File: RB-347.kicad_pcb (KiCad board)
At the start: 2 copper layers, 30 x 55 mm, 34 parts, among them J1 Conn_USB_C_Socket, J2 PINHD_1x10_Male, J3 PINHD_1x10_Male, J4 PINHD_1x10_Male, SW1 I2C, SW2 SPDT_Slide_SMD_6.7x2.6mm, U1 USBLC6-2SC6, U2 CH347F, U3 TLV74333PDBVR, U4 TLV74318PDBVR, Y1 8Mhz

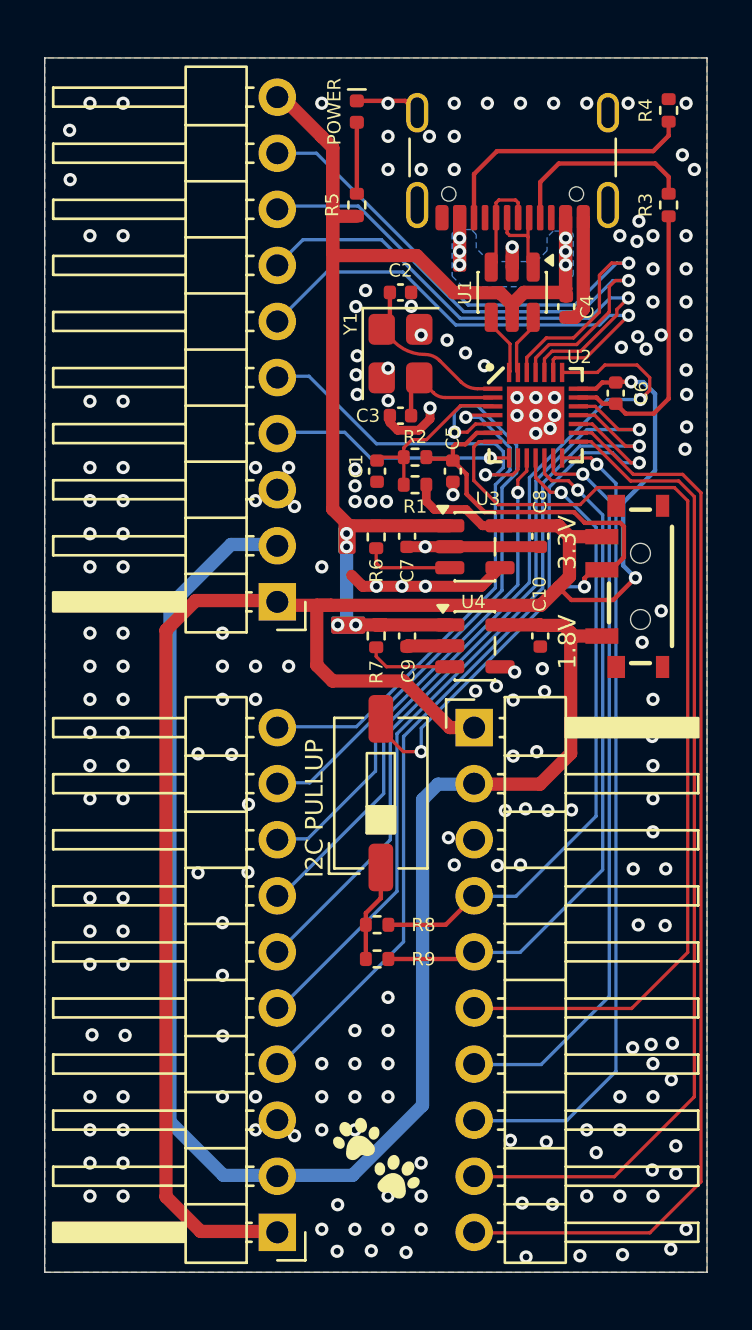
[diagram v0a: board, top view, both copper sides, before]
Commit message: add I²C indicator LED
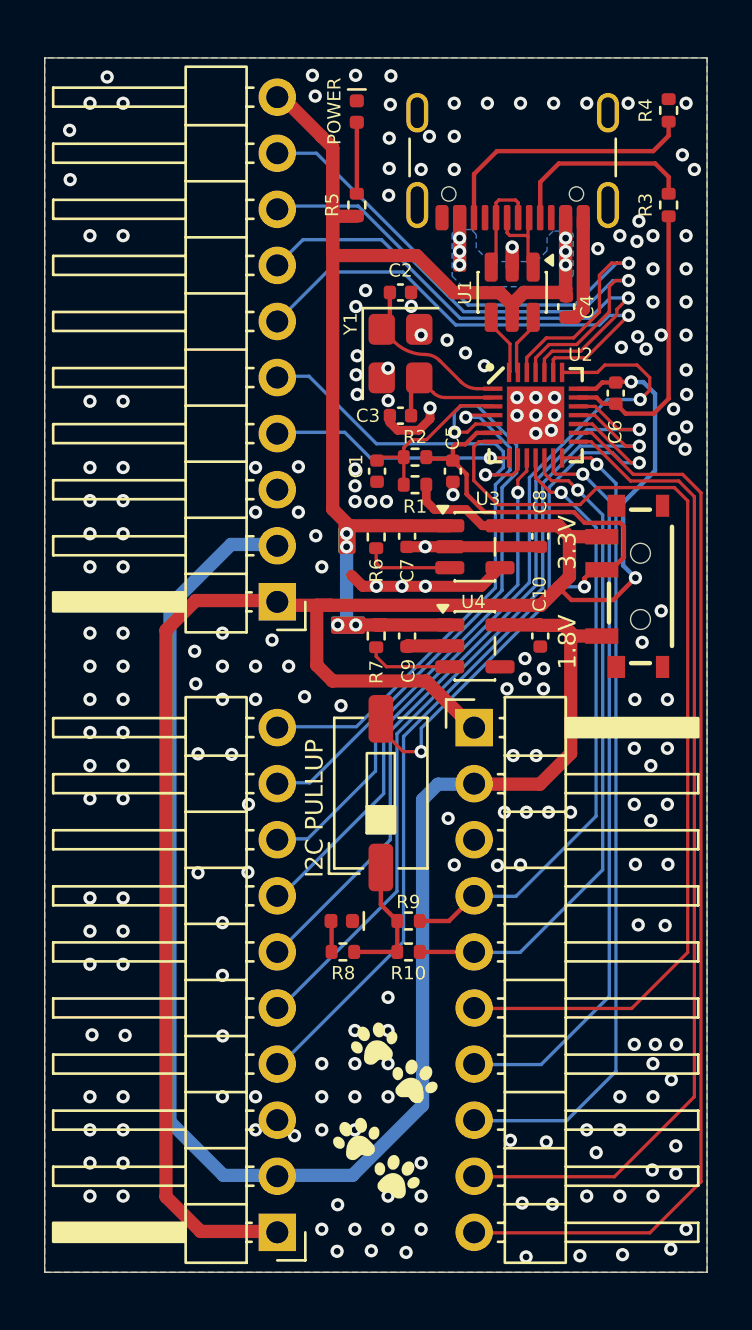
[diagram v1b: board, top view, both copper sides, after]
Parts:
- added G***: LOGO, LOGO, F.Cu at (122.9, 112.8)
- added LED2: POWER, PCM_SparkFun-LED:LED_0402_1005Metric_Red, F.Cu at (120.5, 106.3)
- added R8: 1k, Resistor_SMD:R_0402_1005Metric, F.Cu at (120.6, 107.8)
- moved R10 1.46 mm to (123.6, 107.8)
- moved R9 1.43 mm to (123.6, 106.3)
- renumbered R9 to R10, R8 to R9
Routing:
- net GND: track 41.8 -> 38.9 mm, vias 212 -> 228
- net Net-(R10-Pad1): track 4.47 -> 6.09 mm
- net CTS1/SCL: track 29.1 -> 27.6 mm
- net Net-(LED2-A): track 0.00 -> 1.41 mm
- net RTS1/SDA: track 31.6 -> 30.4 mm

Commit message: change connectors
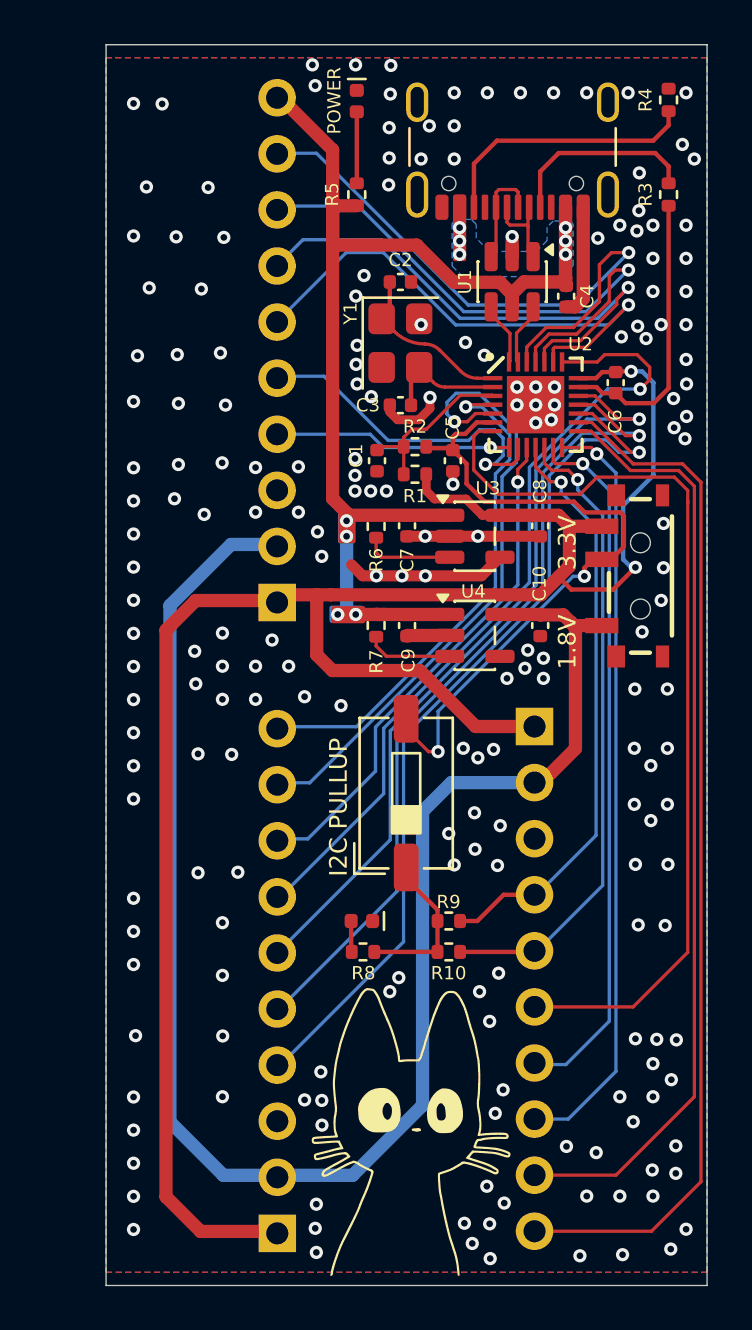
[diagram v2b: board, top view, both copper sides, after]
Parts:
- removed the G*** at (122.1, 117.1)
- removed the G*** at (122.9, 112.8)
- removed the G*** at (121.9, 103.2)
- added G***: LOGO, LOGO, F.Cu at (123.7, 115.9)
- added G***: LOGO, LOGO, B.Cu at (123.4, 114.6)
- J2, J3, J4: footprint Connector_PinHeader_2.54mm:PinHeader_1x10_P2.54mm_Horizontal -> RB-Library:XH_1x10_P2.54mm_Horizontal
- moved J2 2.74 mm to (129.3, 97.5)
- moved R10 1.82 mm to (125.4, 107.8)
- moved R9 1.82 mm to (125.4, 106.3)
- moved SW1 1.15 mm to (123.4, 100.6)
- moved G*** 1.04 mm to (129.2, 84.4)
- moved LED2 0.91 mm to (121.4, 106.3)
- moved R8 0.91 mm to (121.5, 107.8)
- moved R4 0.47 mm to (135.3, 69.2)
- moved R6 0.47 mm to (122.1, 88.5)
- moved SW2 0.47 mm to (134.1, 90.7)
- moved R1 0.47 mm to (123.8, 86.1)
- moved R2 0.47 mm to (123.8, 84.9)
- moved C10 0.47 mm to (129.5, 93.0)
- moved C4 0.47 mm to (130.7, 78.1)
- moved C6 0.47 mm to (132.9, 82.0)
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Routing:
- net VBUS: track 56.1 -> 52.6 mm
- net +3.3V: track 90.9 -> 93.6 mm
- net SCK: track 36.9 -> 34.6 mm
- net MOSI: track 49.1 -> 46.8 mm
- net MISO: track 44.9 -> 42.6 mm
- net DTR1/TNOW1/SCS1: track 44.4 -> 42.2 mm
- net SCS0: track 33.6 -> 31.7 mm
- net Net-(R10-Pad1): track 6.09 -> 7.28 mm
- net RXD1: track 27.0 -> 28.1 mm
- net TCK/SWDCLK/GPIO4: track 22.8 -> 23.8 mm
- net CTS1/SCL: track 27.6 -> 26.8 mm
- net RTS1/SDA: track 30.4 -> 29.8 mm
- net CTS0/GPIO0: track 39.7 -> 40.2 mm
- net RTS0/GPIO1: track 37.2 -> 37.7 mm
- net VIO: track 31.3 -> 30.7 mm
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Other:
- board size 30 x 55 mm -> 27.2 x 56.2 mm
